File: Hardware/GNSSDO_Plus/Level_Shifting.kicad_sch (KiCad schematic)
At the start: 36 parts, among them J3 SMA_Edge, SW4 DPDT_Slide_SMD_7.2x3.5mm, U10 74LVC2T45DC, U12 74LVC2T45DC, U14 74LVC2T45DC, U8 74LVC2T45DC, U9 74LVC2T45DC

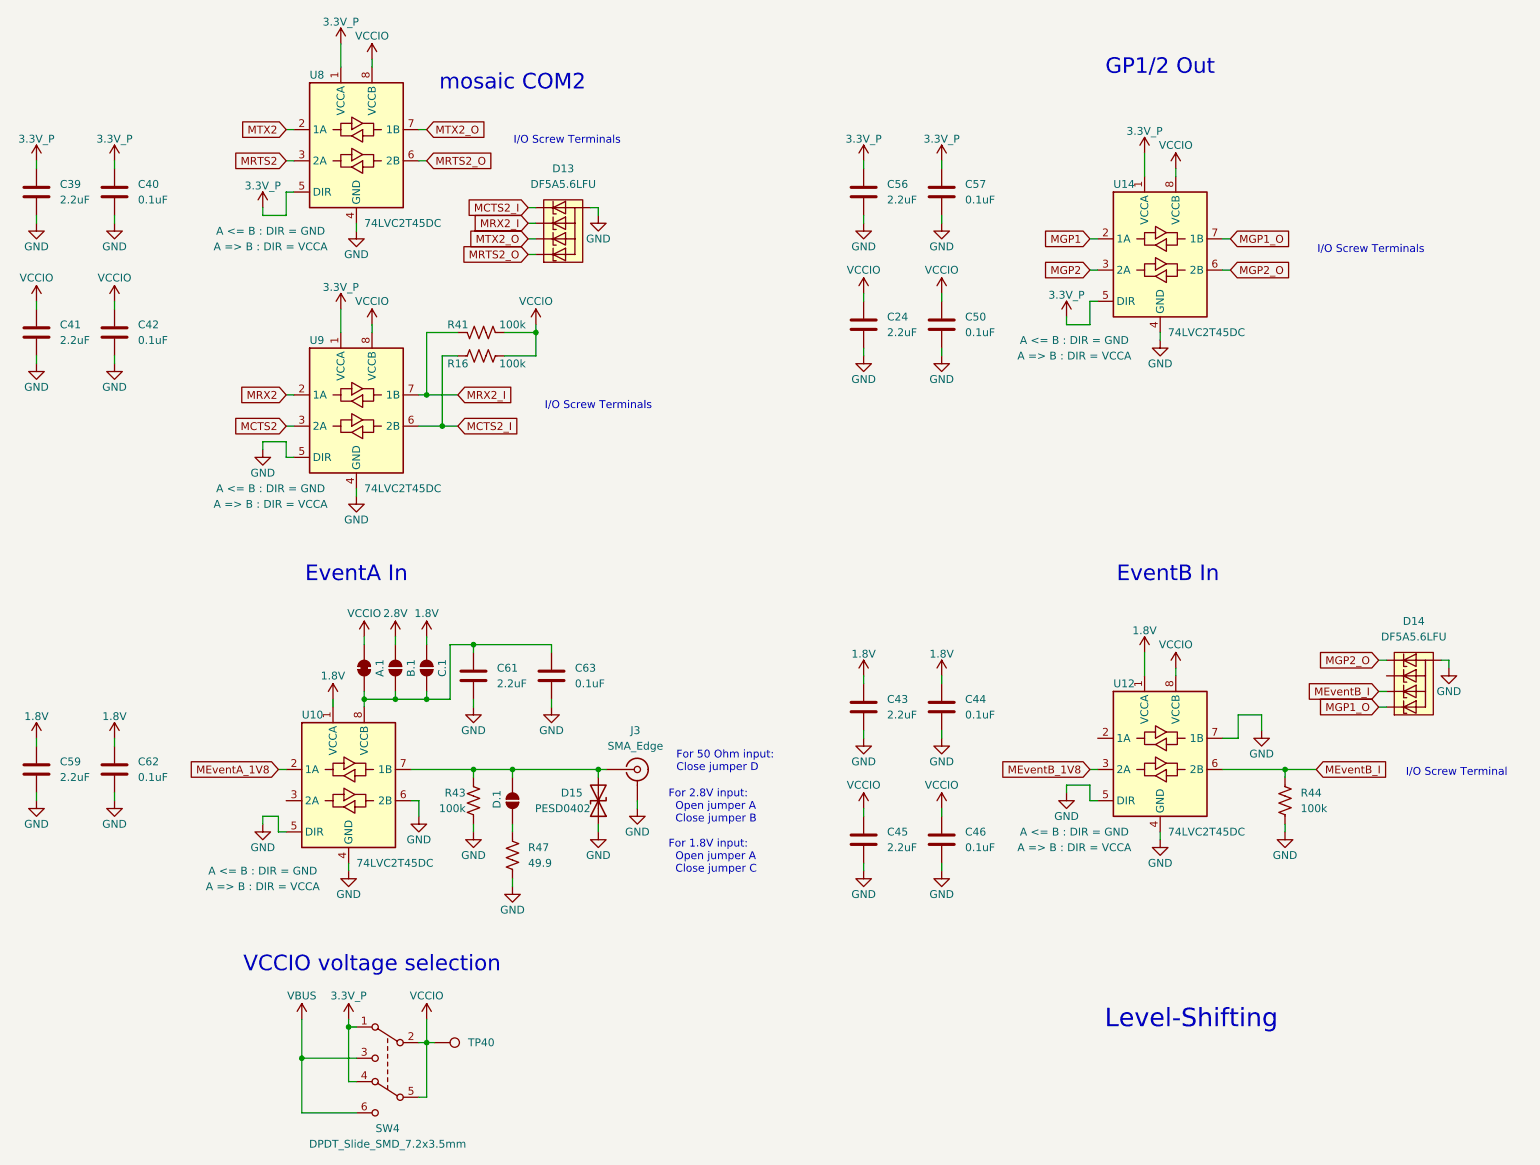
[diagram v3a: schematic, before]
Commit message: GNSSDO+ : update symbols and footprints
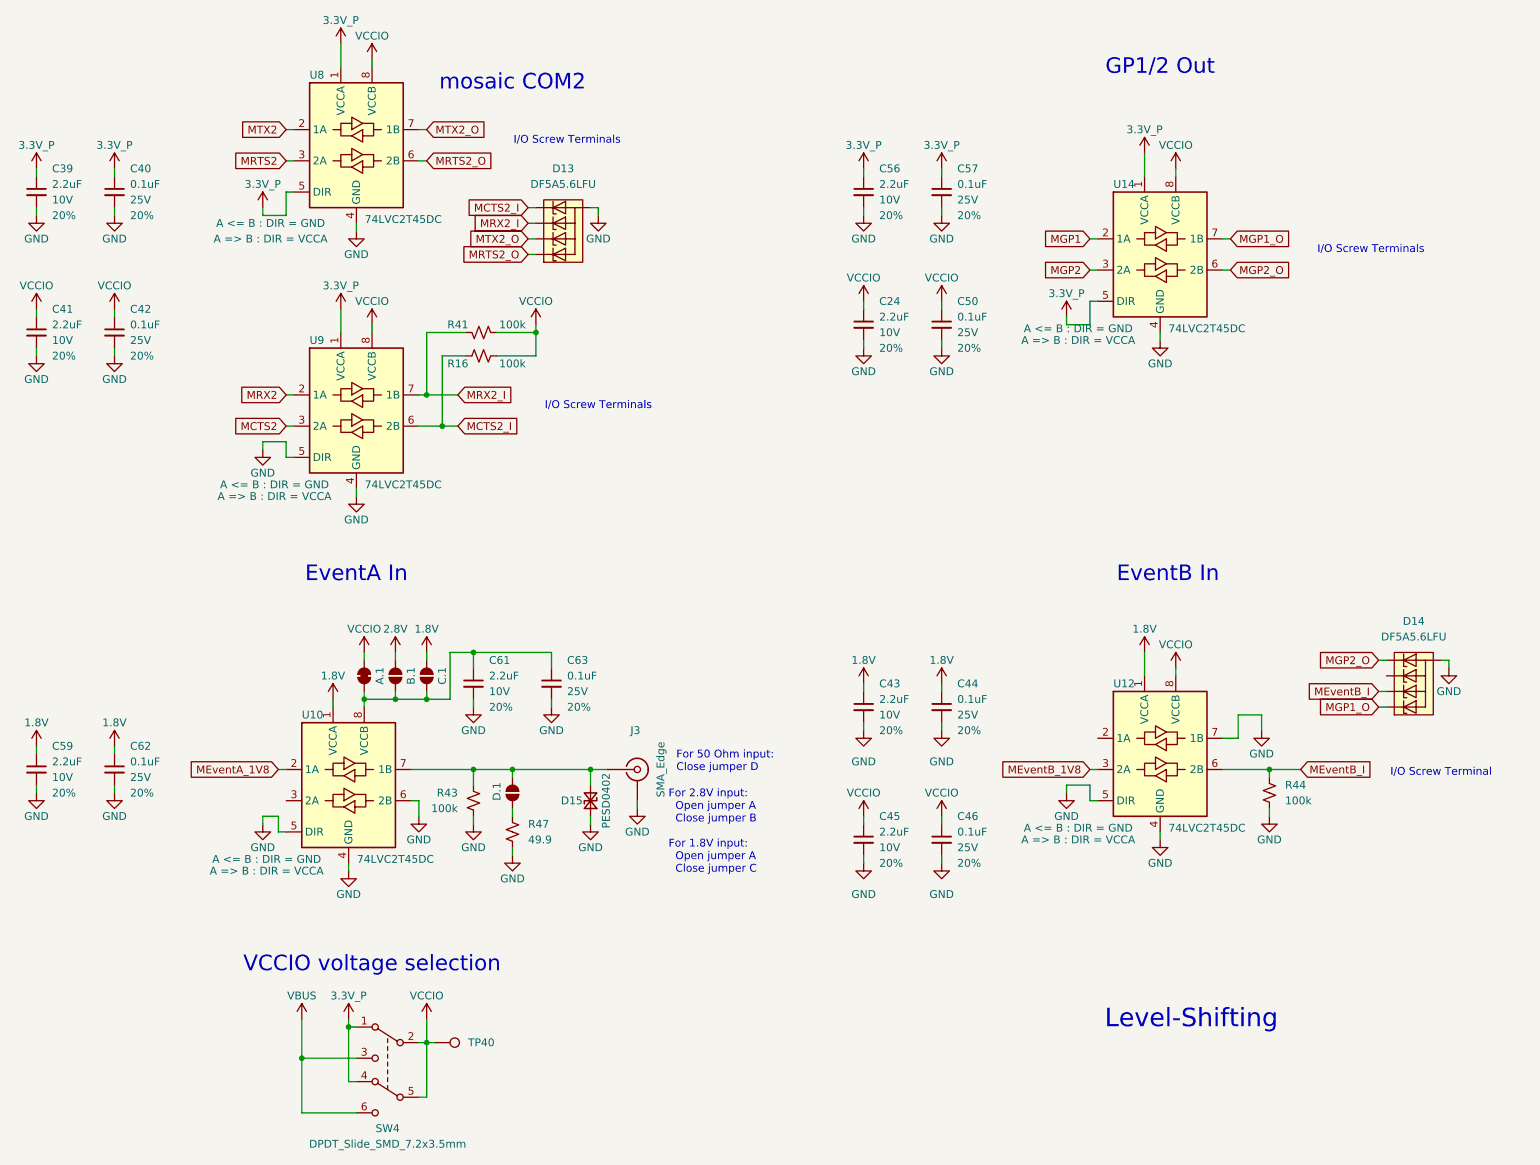
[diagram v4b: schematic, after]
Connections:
- net GND: now also R43.1, R44.1, R47.2; no longer R43.2, R44.2, R47.1
- net MCTS2_I: now also R16.1; no longer R16.2
- net MEventB_I: now also R44.2; no longer R44.1
- net MRX2_I: now also R41.1; no longer R41.2
- net VCCIO: now also R16.2, R41.2; no longer R16.1, R41.1
- net at D.1.1 (A): now also R47.1; no longer R47.2
- net at D.1.2 (B), D15.2 (A2), J3.1 (In)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: now also R43.2; no longer R43.1
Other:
- moved on the sheet: A.1, B.1, C.1, C61, C63, D.1, D15

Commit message: GNSSDO Plus - ready for review
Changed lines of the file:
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@@
 	(text "For 50 Ohm input:\nClose jumper D"
 		(exclude_from_sim no)
-		(at 125.73 137.16 0)
+		(at 102.87 156.21 0)
 		(effects
 			(font
@@
 	(text "For 2.8V input:\n  Open jumper A\n  Close jumper B\n\nFor 1.8V input:\n  Open jumper A\n  Close jumper C"
 		(exclude_from_sim no)
-		(at 124.46 148.59 0)
+		(at 45.72 120.65 0)
 		(effects
 			(font
@@
 		)
 		(property "DIR1" "A <= B : DIR = GND"
-			(at 191.135 66.675 0)
+			(at 191.77 67.31 0)
 			(effects
 				(font
@@
 		)
 		(property "DIR2" "A => B : DIR = VCCA"
-			(at 191.135 68.58 0)
+			(at 191.77 69.85 0)
 			(effects
 				(font
@@
 		(dnp no)
 		(property "Reference" "J3"
-			(at 119.0626 132.08 0)
+			(at 119.38 134.62 0)
 			(effects
 				(font

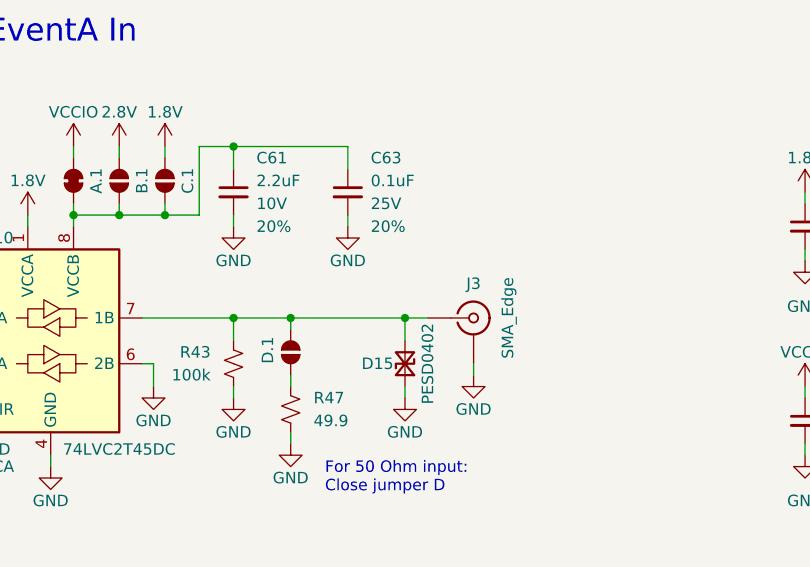
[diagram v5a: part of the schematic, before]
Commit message: GNSSDO+ PCB ready for protos
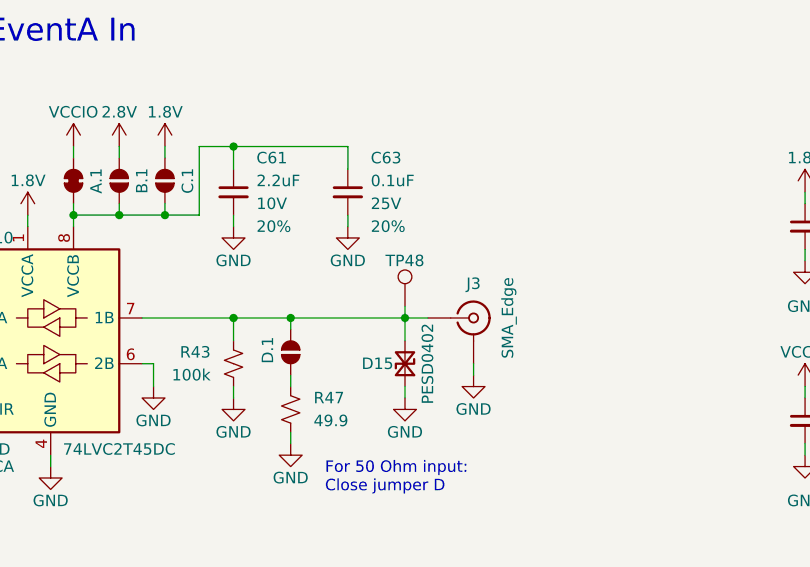
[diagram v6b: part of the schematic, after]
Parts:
- added TP48: 1.25mm, SparkFun-Connector:TestPoint-1.25mm, symbol SparkFun-Connector:TestPoint_1.25mm
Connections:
- net at D.1.2 (B), D15.2 (A2), J3.1 (In)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: now also TP48.1
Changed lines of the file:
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@@
 	(wire
 		(pts
+			(xy 111.76 137.16) (xy 111.76 138.43)
+		)
+		(stroke
+			(width 0)
+			(type default)
+		)
+	)
+	(wire
+		(pts
 			(xy 156.21 41.91) (xy 156.21 40.64)
 		)
@@
 					(unit 1)
 				)
+			)
+		)
+	)
+	(symbol
+		(lib_id "SparkFun-Connector:TestPoint_1.25mm")
+		(at 111.76 137.16 0)
+		(unit 1)
+		(exclude_from_sim no)
+		(in_bom yes)
+		(on_board yes)
+		(dnp no)
+		(fields_autoplaced yes)
+		(property "Reference" "TP48"
+			(at 111.76 132.08 0)
+			(do_not_autoplace yes)
+			(effects
+				(font
+					(size 1.27 1.27)
+				)
+			)
+		)
+		(property "Value" "1.25mm"
+			(at 111.76 140.97 0)
+			(effects
+				(font
+					(size 1.27 1.27)
+				)
+				(hide yes)
+			)
+		)
+		(property "Footprint" "SparkFun-Connector:TestPoint-1.25mm"
+			(at 111.76 143.51 0)
+			(effects
+				(font
+					(size 1.27 1.27)
+				)
+				(hide yes)
+			)
+		)
+		(property "Datasheet" "~"
+			(at 111.76 144.78 0)
+			(effects
+				(font
+					(size 1.27 1.27)
+				)
+				(hide yes)
+			)
+		)
+		(property "Description" "Test Point"
+			(at 111.76 147.32 0)
+			(effects
+				(font
+					(size 1.27 1.27)
+				)
+				(hide yes)
+			)
+		)
+		(pin "1"
+		)
+		(instances
+			(project ""
+				(path "/e3dd3ae4-244d-4cba-9cca-5d2abf83f29a/d9a77ac1-2999-4329-b708-8e6cc1b00c22"
+					(reference "TP48")
+					(unit 1)
+				)

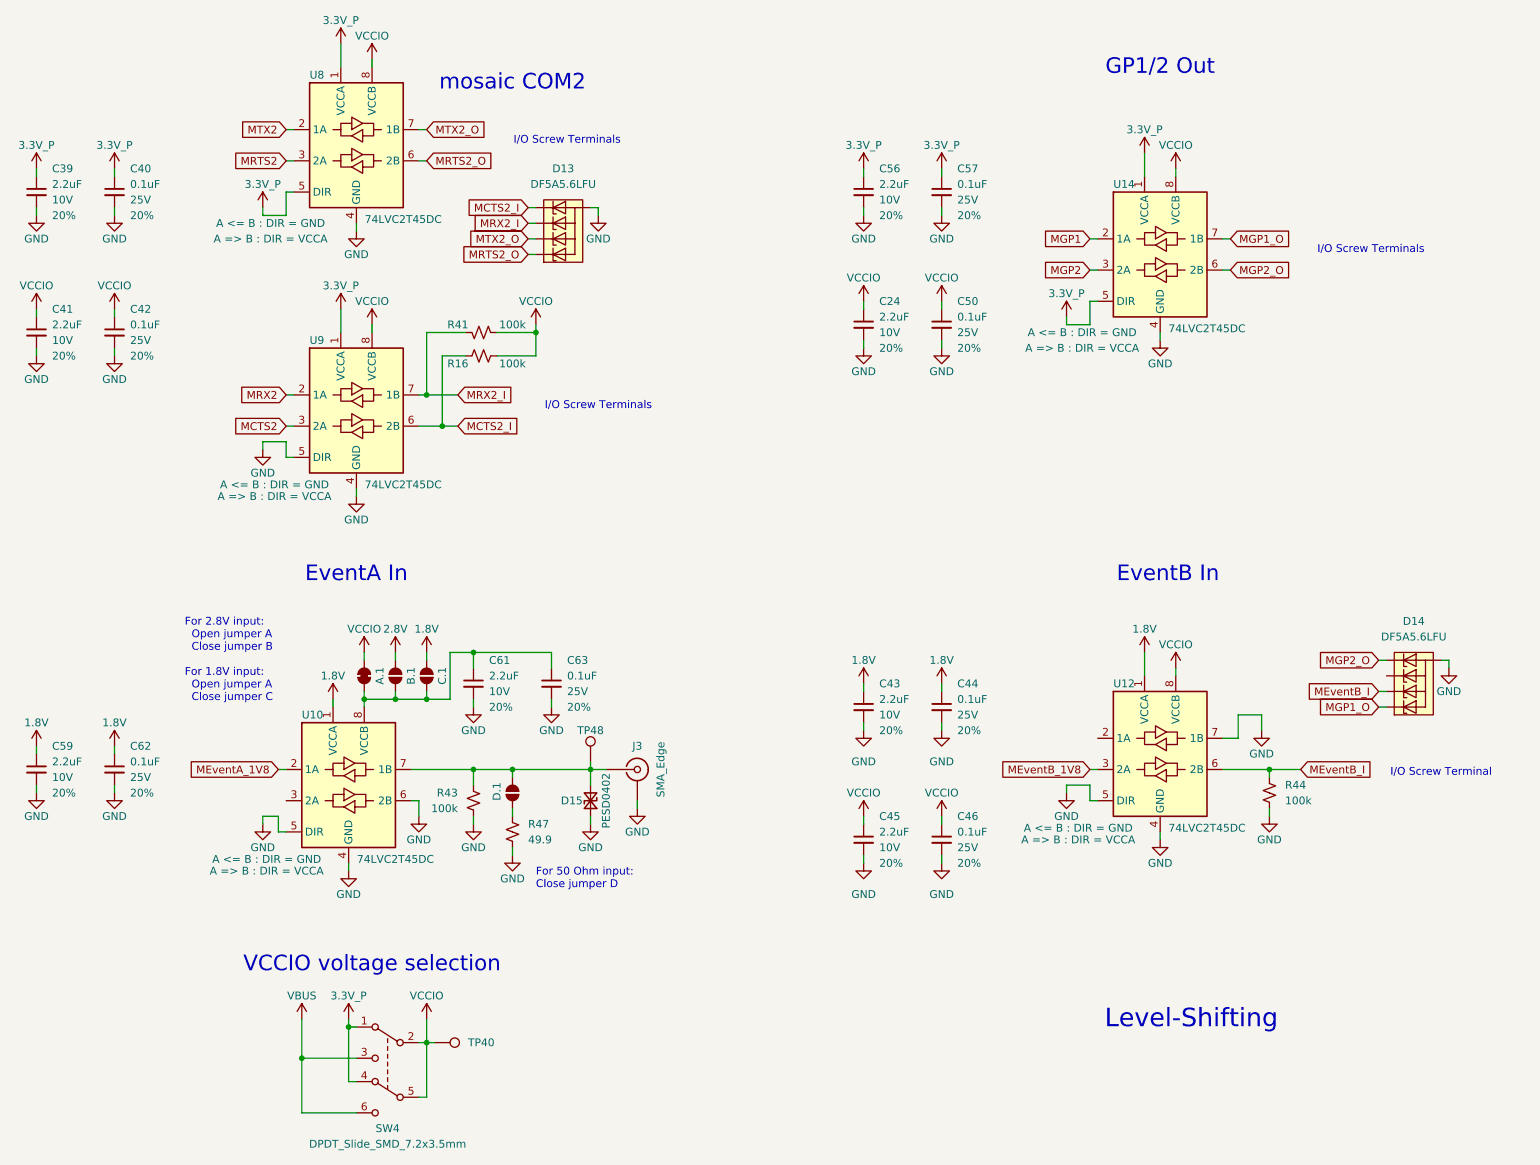
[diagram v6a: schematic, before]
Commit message: GNSSDO+ v02 PCB - with DP5305 PoE module, PowerPath Controllers and MS8607 PHT sensor
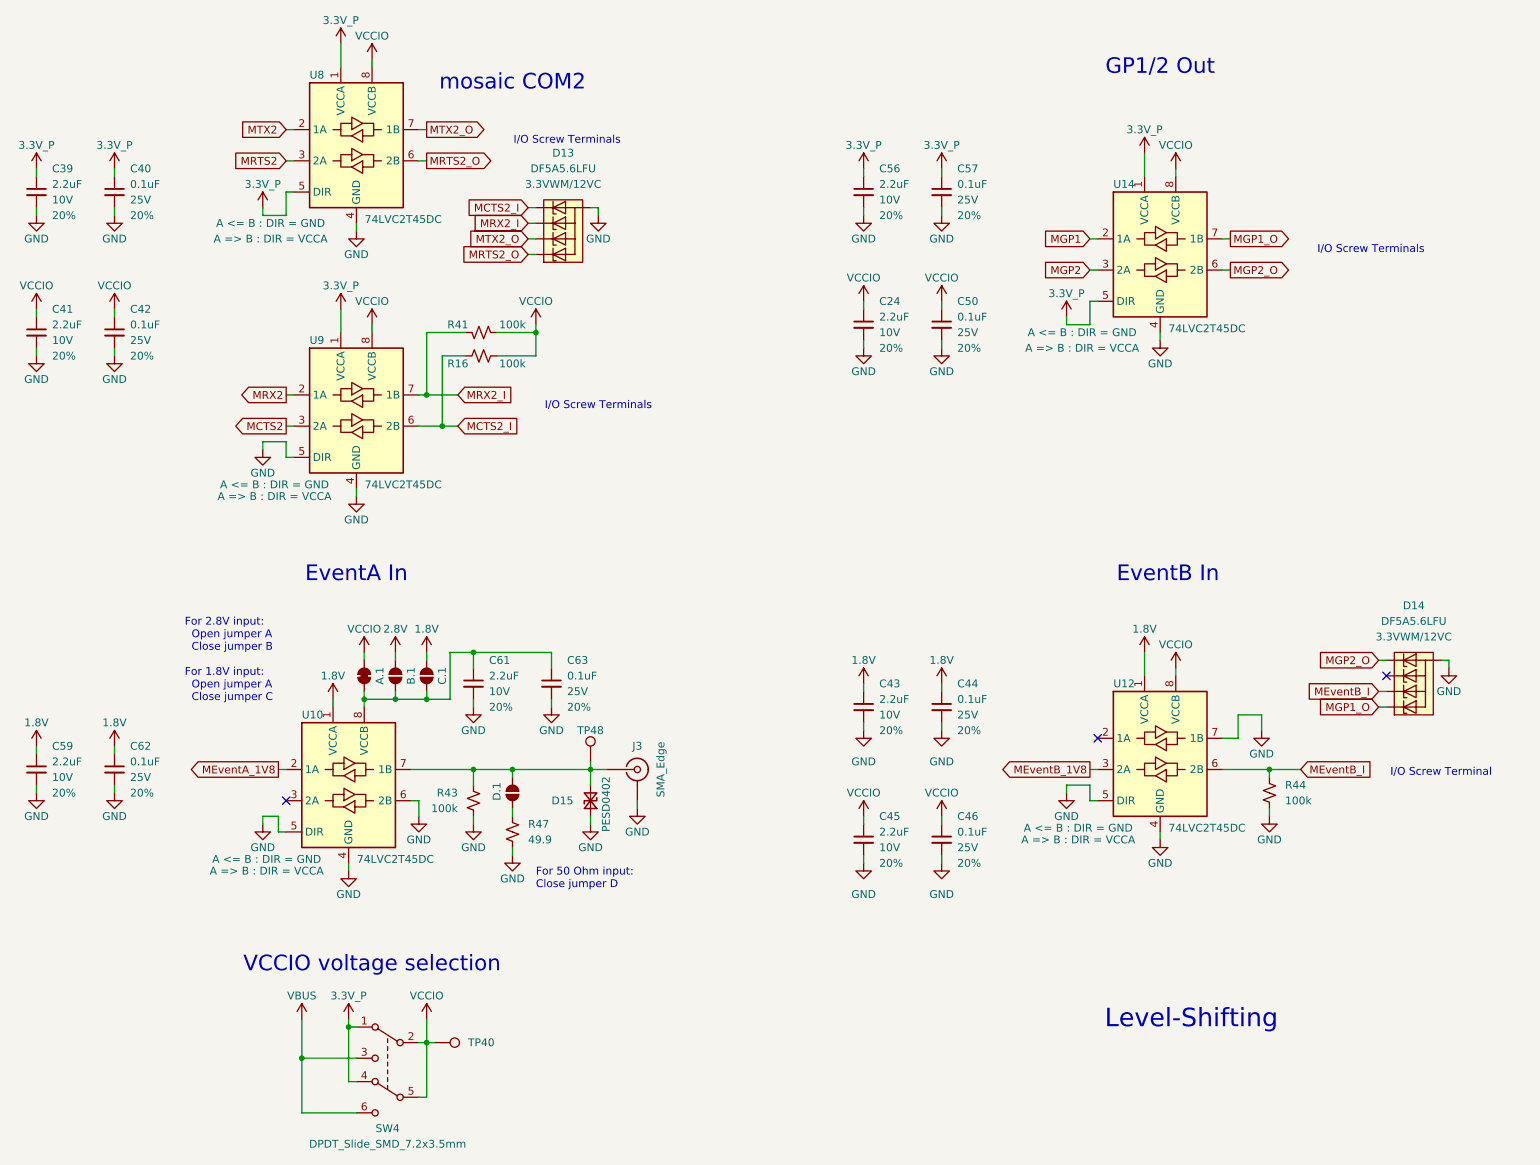
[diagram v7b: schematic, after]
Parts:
- D13, D14: symbol SparkFun-DiscreteSemi:D_TVS_ESD_4_HS -> SparkFun-DiscreteSemi:D_TVS_ESD_4_HS_3.3V; Rating (none) -> 3.3VWM/12VC
- D15: symbol SparkFun-DiscreteSemi:D_TVS_0402 -> SparkFun-DiscreteSemi:D_TVS_0402_14V; Rating (none) -> 14VWM/40VC
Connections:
- no-connect marks 0 -> 3
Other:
- title: Level Shifting -> GNSSDO Plus - Level Shifting

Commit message: Update GNSSDO KiCad files to match latest SparkFun library
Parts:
- C24, C39, C41, C43, C45, C56, C59, C61: PROD_ID CAP-07888 -> CAP-24999
- J3: footprint SparkFun-Connector:SMA_Edge -> SparkFun-Connector:SMA_Edge_6.3mm; symbol SparkFun-RF:SMA_EdgeMount -> SparkFun-RF:SMA_EdgeMount_6.3mm
- TP40: footprint SparkFun-Connector:1x01 -> SparkFun-Connector:1x01_P2.54mm
